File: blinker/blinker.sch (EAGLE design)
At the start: 12 parts, among them IC1 LM555N

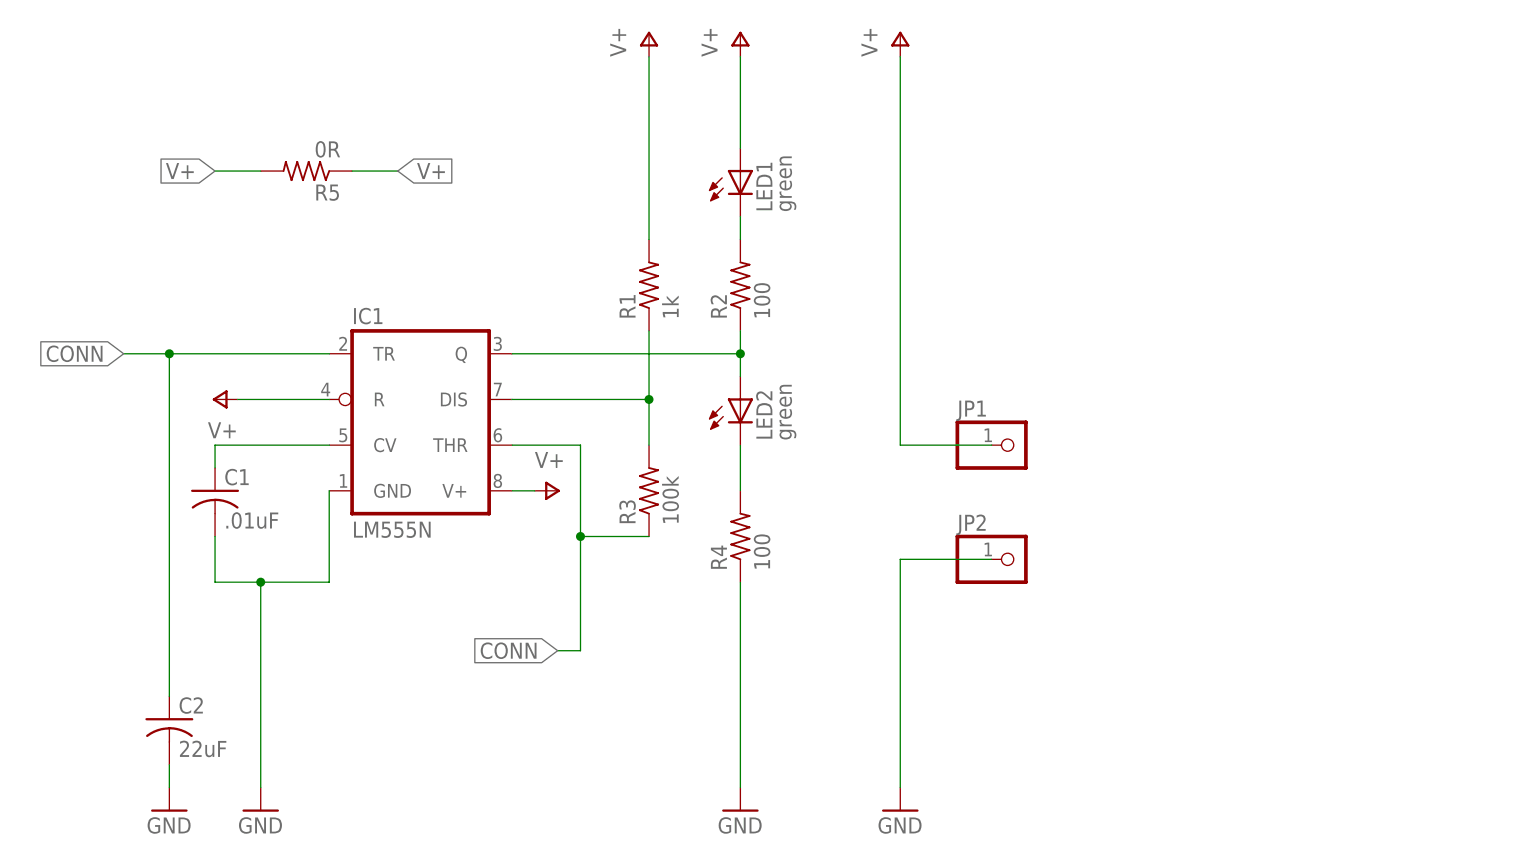
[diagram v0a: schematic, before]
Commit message: Blinker component size changes
Also added gitignore, and some datasheets
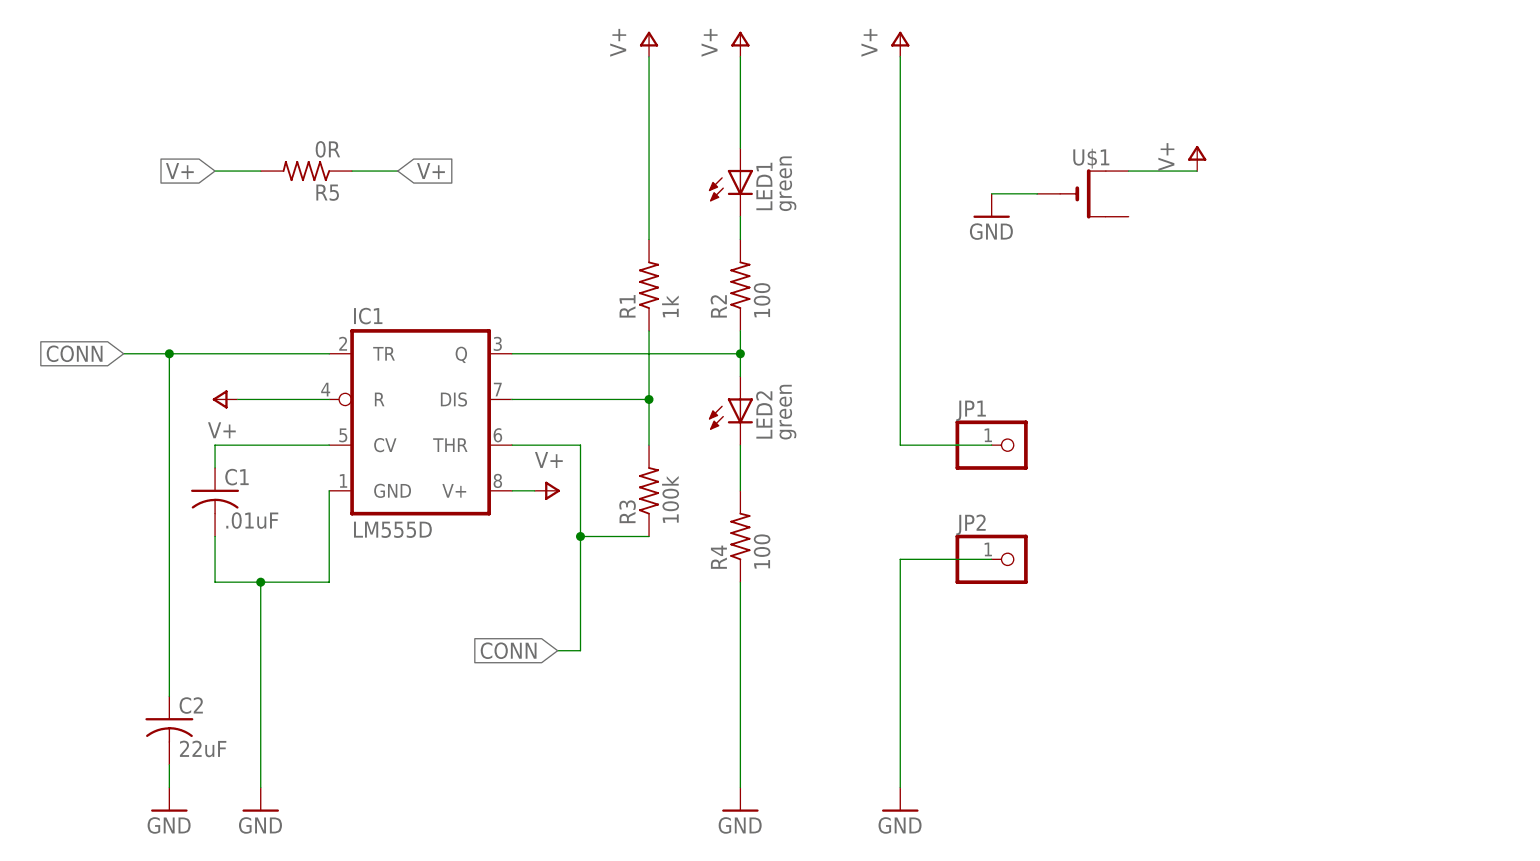
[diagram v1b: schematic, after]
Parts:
- added U$1: (no value), adafruit:CR2032SMT
- C1, C2: device adafruit:C-USC1206 -> adafruit:C-USC0805
- IC1: value LM555N -> LM555D; device adafruit:LM555N -> adafruit:LM555D
- R1, R2, R3, R4: device adafruit:R-US_R1206 -> adafruit:R-US_R0805
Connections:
- net GND: now also U$1.-
- net V+: now also U$1.+
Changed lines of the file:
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@@
 <setting verticaltext="up"/>
 </settings>
-<grid distance="0.1" unitdist="inch" unit="inch" style="lines" multiple="1" display="yes" altdistance="0.01" altunitdist="inch" altunit="inch"/>
+<grid distance="0.1" unitdist="inch" unit="inch" style="lines" multiple="1" display="no" altdistance="0.01" altunitdist="inch" altunit="inch"/>
 <layers>
 <layer number="1" name="Top" color="4" fill="1" visible="no" active="no"/>
@@
 <layer number="49" name="Reference" color="7" fill="1" visible="no" active="no"/>
 <layer number="50" name="dxf" color="7" fill="1" visible="no" active="no"/>
-<layer number="51" name="tDocu" color="6" fill="1" visible="no" active="no"/>
+<layer number="51" name="tDocu" color="7" fill="1" visible="no" active="no"/>
 <layer number="52" name="bDocu" color="7" fill="1" visible="no" active="no"/>
 <layer number="53" name="tGND_GNDA" color="7" fill="9" visible="no" active="no"/>
@@
 </classes>
 <parts>
-<part name="IC1" library="adafruit" deviceset="*555" device="N" technology="LM"/>
-<part name="R1" library="adafruit" deviceset="R-US_" device="R1206" value="1k"/>
-<part name="R2" library="adafruit" deviceset="R-US_" device="R1206" value="100"/>
-<part name="R3" library="adafruit" deviceset="R-US_" device="R1206" value="100k"/>
-<part name="R4" library="adafruit" deviceset="R-US_" device="R1206" value="100"/>
+<part name="IC1" library="adafruit" deviceset="*555" device="D" technology="LM" value="LM555D"/>
+<part name="R1" library="adafruit" deviceset="R-US_" device="R0805" value="1k"/>
+<part name="R2" library="adafruit" deviceset="R-US_" device="R0805" value="100"/>
+<part name="R3" library="adafruit" deviceset="R-US_" device="R0805" value="100k"/>
+<part name="R4" library="adafruit" deviceset="R-US_" device="R0805" value="100"/>
 <part name="LED1" library="adafruit" deviceset="LED" device="SMT1206" value="green"/>
 <part name="LED2" library="adafruit" deviceset="LED" device="SMT1206" value="green"/>
@@
 <part name="JP1" library="adafruit" deviceset="PINHD-1X1" device="CB"/>
 <part name="JP2" library="adafruit" deviceset="PINHD-1X1" device="CB"/>
-<part name="C1" library="adafruit" deviceset="C-US" device="C1206" value=".01uF"/>
-<part name="C2" library="adafruit" deviceset="C-US" device="C1206" value="22uF"/>
+<part name="C1" library="adafruit" deviceset="C-US" device="C0805" value=".01uF"/>
+<part name="C2" library="adafruit" deviceset="C-US" device="C0805" value="22uF"/>
 <part name="GND3" library="supply1" deviceset="GND" device=""/>
 <part name="GND4" library="supply1" deviceset="GND" device=""/>
@@
 <part name="P+5" library="supply1" deviceset="V+" device=""/>
 <part name="R5" library="adafruit" deviceset="R-US_" device="R1206" value="0R"/>
+<part name="U$1" library="adafruit" deviceset="CR2032" device="SMT"/>
+<part name="P+6" library="supply1" deviceset="V+" device=""/>
+<part name="GND5" library="supply1" deviceset="GND" device=""/>
 </parts>
 <sheets>
@@
 <instance part="P+5" gate="1" x="86.36" y="88.9"/>
 <instance part="R5" gate="G$1" x="20.32" y="73.66" rot="R180"/>
+<instance part="U$1" gate="G$1" x="106.68" y="71.12"/>
+<instance part="P+6" gate="1" x="119.38" y="76.2"/>
+<instance part="GND5" gate="1" x="96.52" y="68.58"/>
 </instances>
 <busses>
@@
 <junction x="15.24" y="27.94"/>
 </segment>
+<segment>
+<pinref part="U$1" gate="G$1" pin="-"/>
+<wire x1="101.6" y1="71.12" x2="96.52" y2="71.12" width="0.1524" layer="91"/>
+<pinref part="GND5" gate="1" pin="GND"/>
+</segment>
 </net>
 <net name="CONN" class="0">
@@
 <label x="30.48" y="73.66" size="1.778" layer="95" xref="yes"/>
 </segment>
-</net>
+<segment>
+<pinref part="U$1" gate="G$1" pin="+"/>
+<wire x1="111.76" y1="73.66" x2="119.38" y2="73.66" width="0.1524" layer="91"/>
+<pinref part="P+6" gate="1" pin="V+"/>
+</segment>
+</net>

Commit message: PCB design is ready for Blinker
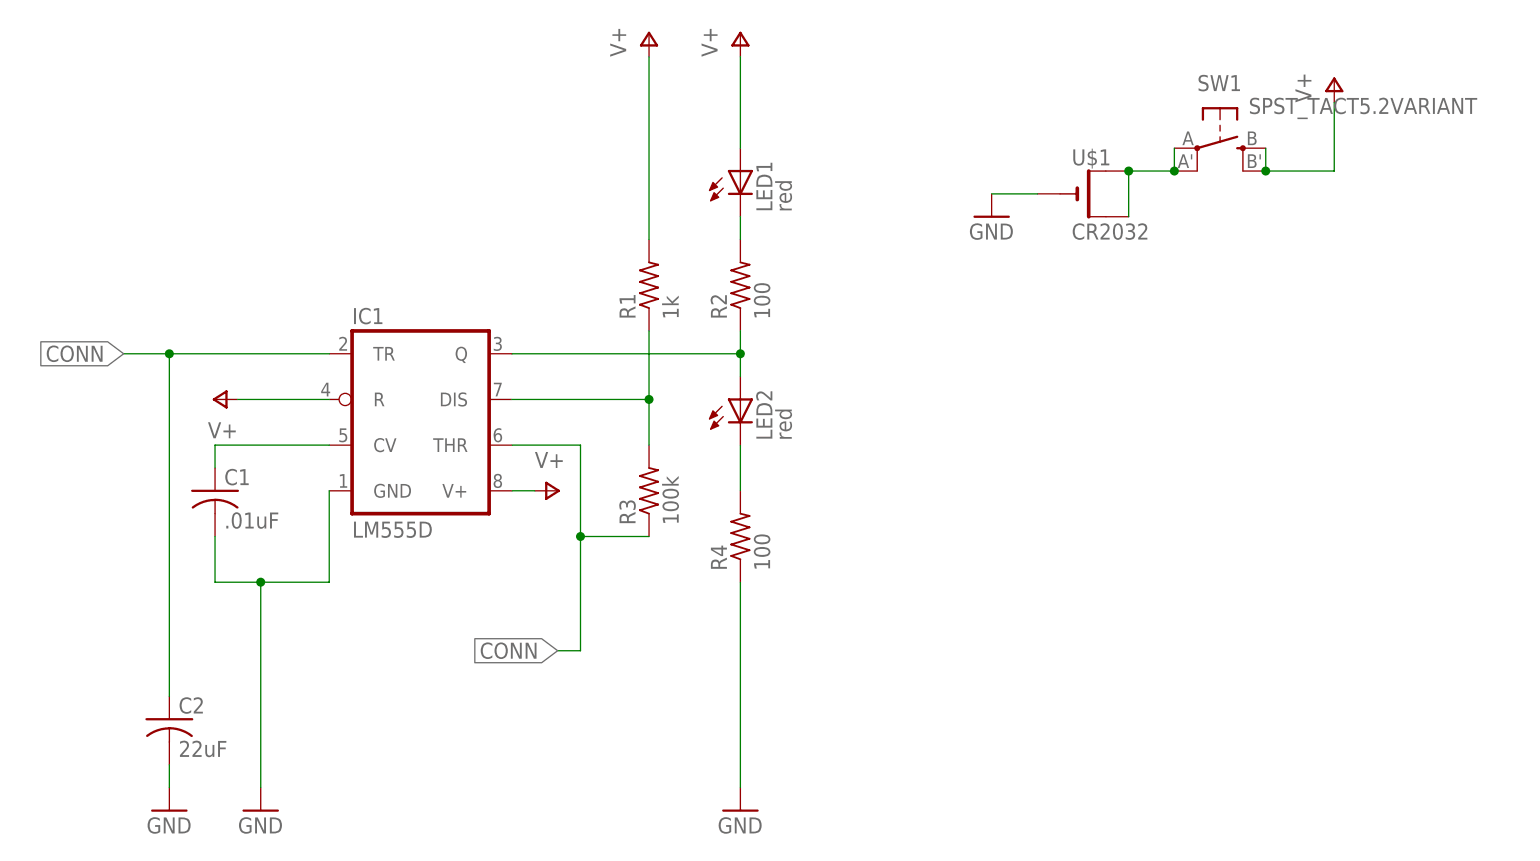
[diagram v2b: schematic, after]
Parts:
- removed JP1, JP2: (no value), adafruit:PINHD-1X1CB
- removed R5: 0R, adafruit:R-US_R1206
- added SW1: SPST_TACT5.2VARIANT, mokerek:SPST_TACT5.2VARIANT
- LED1, LED2: value green -> red; device adafruit:LEDSMT1206 -> adafruit:LEDCHIPLED_0805
- U$1: value (none) -> CR2032
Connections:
- new net N$6: SW1.P, SW1.P1, U$1.+, U$1.+1
- net GND: no longer JP2.1
- net V+: now also SW1.S, SW1.S1; no longer JP1.1, R5.1, R5.2, U$1.+

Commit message: CR2032 Batt holder amended, PCB design update
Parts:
- U$1: device adafruit:CR2032SMT -> mokerek:CR2032SMT
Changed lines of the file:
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@@
 <grid distance="0.1" unitdist="inch" unit="inch" style="lines" multiple="1" display="no" altdistance="0.01" altunitdist="inch" altunit="inch"/>
 <layers>
-<layer number="1" name="Top" color="4" fill="1" visible="yes" active="no"/>
-<layer number="16" name="Bottom" color="1" fill="1" visible="yes" active="no"/>
-<layer number="17" name="Pads" color="2" fill="1" visible="yes" active="no"/>
-<layer number="18" name="Vias" color="2" fill="1" visible="yes" active="no"/>
-<layer number="19" name="Unrouted" color="6" fill="1" visible="yes" active="no"/>
-<layer number="20" name="Dimension" color="15" fill="1" visible="yes" active="no"/>
-<layer number="21" name="tPlace" color="7" fill="1" visible="yes" active="no"/>
-<layer number="22" name="bPlace" color="7" fill="1" visible="yes" active="no"/>
-<layer number="23" name="tOrigins" color="15" fill="1" visible="yes" active="no"/>
-<layer number="24" name="bOrigins" color="15" fill="1" visible="yes" active="no"/>
-<layer number="25" name="tNames" color="7" fill="1" visible="yes" active="no"/>
-<layer number="26" name="bNames" color="7" fill="1" visible="yes" active="no"/>
-<layer number="27" name="tValues" color="7" fill="1" visible="yes" active="no"/>
-<layer number="28" name="bValues" color="7" fill="1" visible="yes" active="no"/>
+<layer number="1" name="Top" color="4" fill="1" visible="no" active="no"/>
+<layer number="16" name="Bottom" color="1" fill="1" visible="no" active="no"/>
+<layer number="17" name="Pads" color="2" fill="1" visible="no" active="no"/>
+<layer number="18" name="Vias" color="2" fill="1" visible="no" active="no"/>
+<layer number="19" name="Unrouted" color="6" fill="1" visible="no" active="no"/>
+<layer number="20" name="Dimension" color="15" fill="1" visible="no" active="no"/>
+<layer number="21" name="tPlace" color="7" fill="1" visible="no" active="no"/>
+<layer number="22" name="bPlace" color="7" fill="1" visible="no" active="no"/>
+<layer number="23" name="tOrigins" color="15" fill="1" visible="no" active="no"/>
+<layer number="24" name="bOrigins" color="15" fill="1" visible="no" active="no"/>
+<layer number="25" name="tNames" color="7" fill="1" visible="no" active="no"/>
+<layer number="26" name="bNames" color="7" fill="1" visible="no" active="no"/>
+<layer number="27" name="tValues" color="7" fill="1" visible="no" active="no"/>
+<layer number="28" name="bValues" color="7" fill="1" visible="no" active="no"/>
 <layer number="29" name="tStop" color="7" fill="3" visible="no" active="no"/>
 <layer number="30" name="bStop" color="7" fill="6" visible="no" active="no"/>
@@
 <layer number="35" name="tGlue" color="7" fill="4" visible="no" active="no"/>
 <layer number="36" name="bGlue" color="7" fill="5" visible="no" active="no"/>
-<layer number="37" name="tTest" color="7" fill="1" visible="yes" active="no"/>
-<layer number="38" name="bTest" color="7" fill="1" visible="yes" active="no"/>
+<layer number="37" name="tTest" color="7" fill="1" visible="no" active="no"/>
+<layer number="38" name="bTest" color="7" fill="1" visible="no" active="no"/>
 <layer number="39" name="tKeepout" color="4" fill="11" visible="no" active="no"/>
 <layer number="40" name="bKeepout" color="1" fill="11" visible="no" active="no"/>
@@
 <layer number="44" name="Drills" color="7" fill="1" visible="no" active="no"/>
 <layer number="45" name="Holes" color="7" fill="1" visible="no" active="no"/>
-<layer number="46" name="Milling" color="3" fill="1" visible="yes" active="no"/>
-<layer number="47" name="Measures" color="7" fill="1" visible="yes" active="no"/>
-<layer number="48" name="Document" color="7" fill="1" visible="yes" active="no"/>
-<layer number="49" name="Reference" color="7" fill="1" visible="yes" active="no"/>
-<layer number="50" name="dxf" color="7" fill="1" visible="yes" active="no"/>
-<layer number="51" name="tDocu" color="7" fill="1" visible="yes" active="no"/>
-<layer number="52" name="bDocu" color="7" fill="1" visible="yes" active="no"/>
-<layer number="53" name="tGND_GNDA" color="7" fill="9" visible="yes" active="no"/>
-<layer number="54" name="bGND_GNDA" color="1" fill="9" visible="yes" active="no"/>
-<layer number="56" name="wert" color="7" fill="1" visible="yes" active="no"/>
-<layer number="57" name="tCAD" color="7" fill="1" visible="yes" active="no"/>
-<layer number="59" name="tCarbon" color="7" fill="1" visible="yes" active="no"/>
-<layer number="60" name="bCarbon" color="7" fill="1" visible="yes" active="no"/>
+<layer number="46" name="Milling" color="3" fill="1" visible="no" active="no"/>
+<layer number="47" name="Measures" color="7" fill="1" visible="no" active="no"/>
+<layer number="48" name="Document" color="7" fill="1" visible="no" active="no"/>
+<layer number="49" name="Reference" color="7" fill="1" visible="no" active="no"/>
+<layer number="50" name="dxf" color="7" fill="1" visible="no" active="no"/>
+<layer number="51" name="tDocu" color="7" fill="1" visible="no" active="no"/>
+<layer number="52" name="bDocu" color="7" fill="1" visible="no" active="no"/>
+<layer number="53" name="tGND_GNDA" color="7" fill="9" visible="no" active="no"/>
+<layer number="54" name="bGND_GNDA" color="1" fill="9" visible="no" active="no"/>
+<layer number="56" name="wert" color="7" fill="1" visible="no" active="no"/>
+<layer number="57" name="tCAD" color="7" fill="1" visible="no" active="no"/>
+<layer number="59" name="tCarbon" color="7" fill="1" visible="no" active="no"/>
+<layer number="60" name="bCarbon" color="7" fill="1" visible="no" active="no"/>
 <layer number="90" name="Modules" color="5" fill="1" visible="yes" active="yes"/>
 <layer number="91" name="Nets" color="2" fill="1" visible="yes" active="yes"/>
@@
 <part name="P+3" library="supply1" deviceset="V+" device=""/>
 <part name="P+4" library="supply1" deviceset="V+" device=""/>
-<part name="U$1" library="adafruit" deviceset="CR2032" device="SMT" value="CR2032"/>
+<part name="U$1" library="mokerek" deviceset="CR2032" device="SMT" value="CR2032"/>
 <part name="P+6" library="supply1" deviceset="V+" device=""/>
 <part name="GND5" library="supply1" deviceset="GND" device=""/>
